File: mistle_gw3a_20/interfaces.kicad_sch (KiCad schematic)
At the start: 60 parts, among them J11 Joystick 0, J12 Joystick 1, J4 Micro_SD_Card_Det1, J5 HDMI_A, J6 Grove 1125S-4P, J8 EXT UART, SW2 KEY1, SW3 KEY2, U10 74LCX07, U9 74LCX07

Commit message: Update gw3a dev board
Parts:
- removed R13, R14: 330, Resistor_SMD:R_0402_1005Metric, symbol Device:R_Small
- removed R15, R16: 1k, Resistor_SMD:R_0402_1005Metric, symbol Device:R_Small
- removed SW2: KEY1, Button_Switch_SMD:SW_SPST_TL3342, symbol Switch:SW_Push
- removed SW3: KEY2, Button_Switch_SMD:SW_SPST_TL3342, symbol Switch:SW_Push
- added R22: 1k, Resistor_SMD:R_0402_1005Metric, symbol Device:R_Small
- added R33: 330, Resistor_SMD:R_0402_1005Metric, symbol Device:R_Small
- added SW4: KEY1, Button_Switch_SMD:SW_SPST_TL3342, symbol Switch:SW_Push
- added unit 9 of U7
- added unit 10 of U7
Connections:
- net +3.3V: now also R33.1; no longer D5.4 (VDD)
- net +5V: now also D5.4 (VDD)
- net CK+: now also U7.129 (IOL21A)
- net CK-: now also U7.130 (IOL21B)
- net D0+: now also U7.131 (IOL23A)
- net D0-: now also U7.134 (IOL23B)
- net D1+: now also U7.133 (IOL25A)
- net D1-: now also U7.135 (IOL25B)
- net D2+: now also U7.136 (IOL27A)
- net D2-: now also U7.137 (IOL27B)
- net GND: now also R22.2
- net JOYA0: now also U7.112 (IOL3A/GCLKT_14/LPLL0_T_IN2/LPLL0_T_FB0)
- net JOYA1: now also U7.111 (IOL3B/GCLKC_14/LPLL0_C_IN2/LPLL0_C_FB0)
- net JOYA2: now also U7.114 (IOL5A/GCLKT_13/LPLL0_T_IN1/LPLL0_T_FB1)
- net JOYA3: now also U7.113 (IOL5B/GCLKC_13/LPLL0_C_IN1/LPLL0_C_FB1)
- net JOYA4: now also U7.116 (IOL7A)
- net JOYA5: now also U7.115 (IOL7B)
- net JOYB0: now also U7.118 (IOL9A)
- net JOYB1: now also U7.119 (IOL9B)
- net JOYB2: now also U7.120 (IOL12A)
- net JOYB3: now also U7.121 (IOL12B)
- net JOYB4: now also U7.122 (IOL14A/LPLL1_T_IN1/LPLL1_T_FB1)
- net JOYB5: now also U7.123 (IOL14B/LPLL1_C_IN1/LPLL1_C_FB1)
- net LED0: now also U7.105 (IOT3A/GCLKT_16)
- net LED1: now also U7.106 (IOT3B/GCLKC_16)
- net LED2: now also U7.104 (IOT5A)
- net LED3: now also U7.102 (IOT19A)
- net LED4: now also U7.101 (IOT19B)
- net LED5: now also U7.99 (IOT25A)
- net MON_RX: now also U7.98 (IOT25B)
- net WS2812: now also U7.97 (IOT27A)
- new net: R33.2, SW4.1
- new net ~{USER}: R22.1, SW4.2, U7.96 (IOT27B)
- no-connect marks 3 -> 7
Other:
- moved on the sheet: C18, C19, C20, C21, C22, C23, C24, C25, C26, C40, C45, C58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

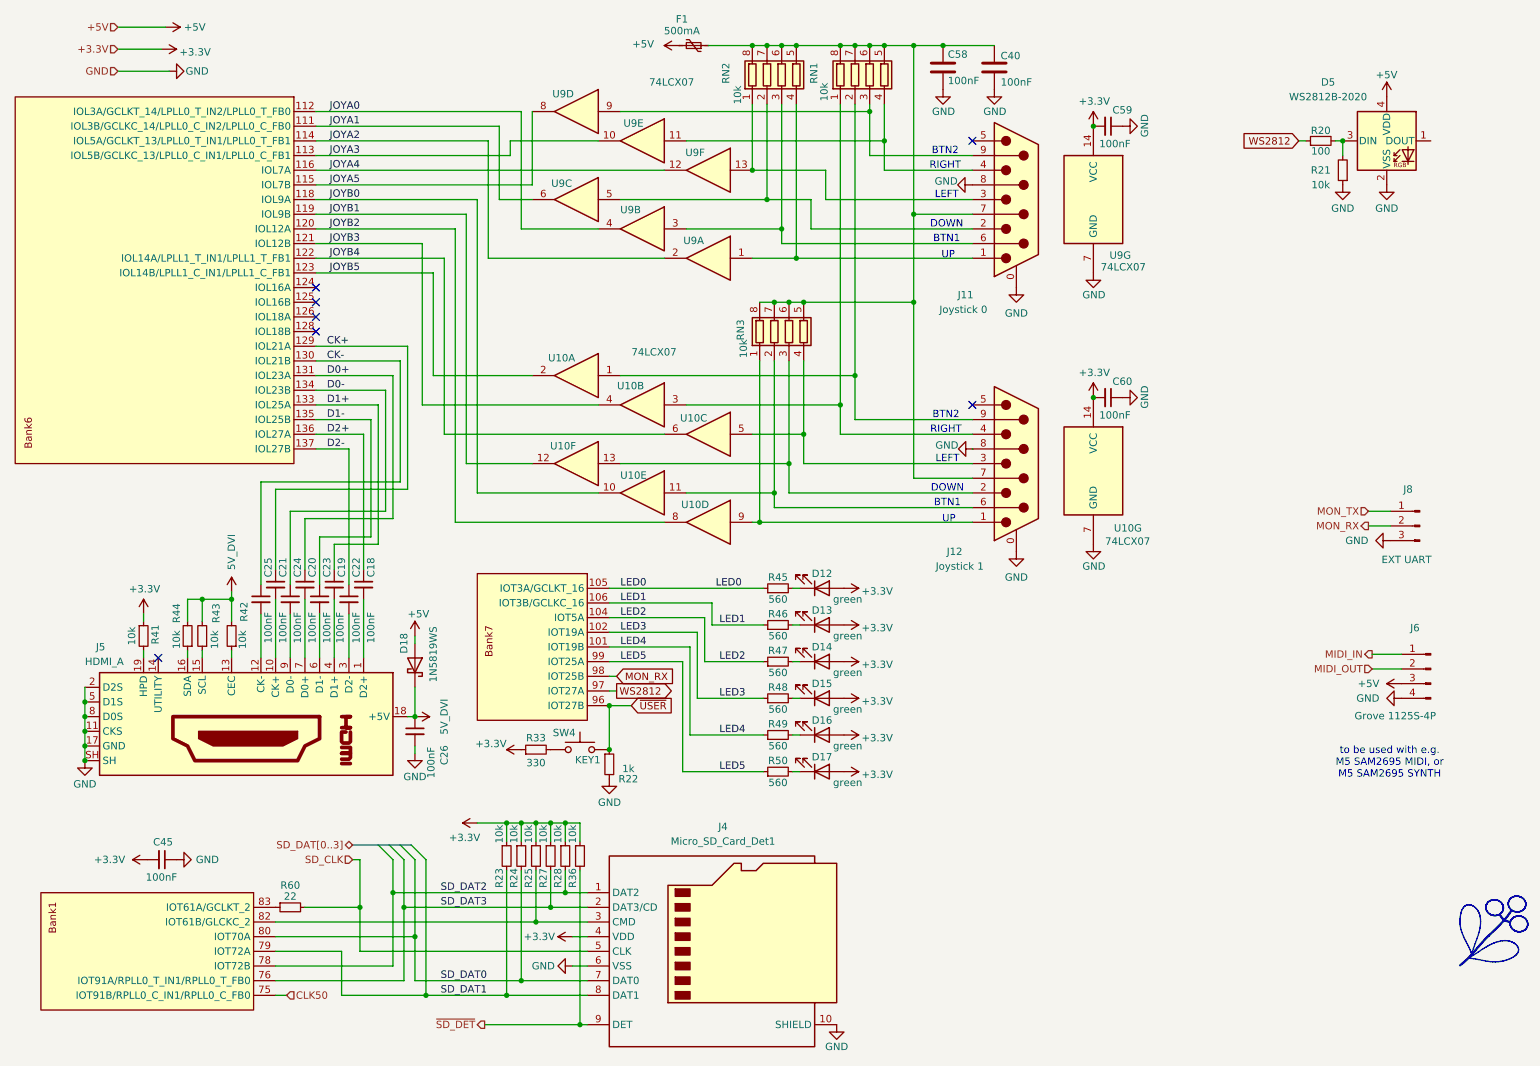
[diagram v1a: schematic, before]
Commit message: Update gw3a 20 dev board
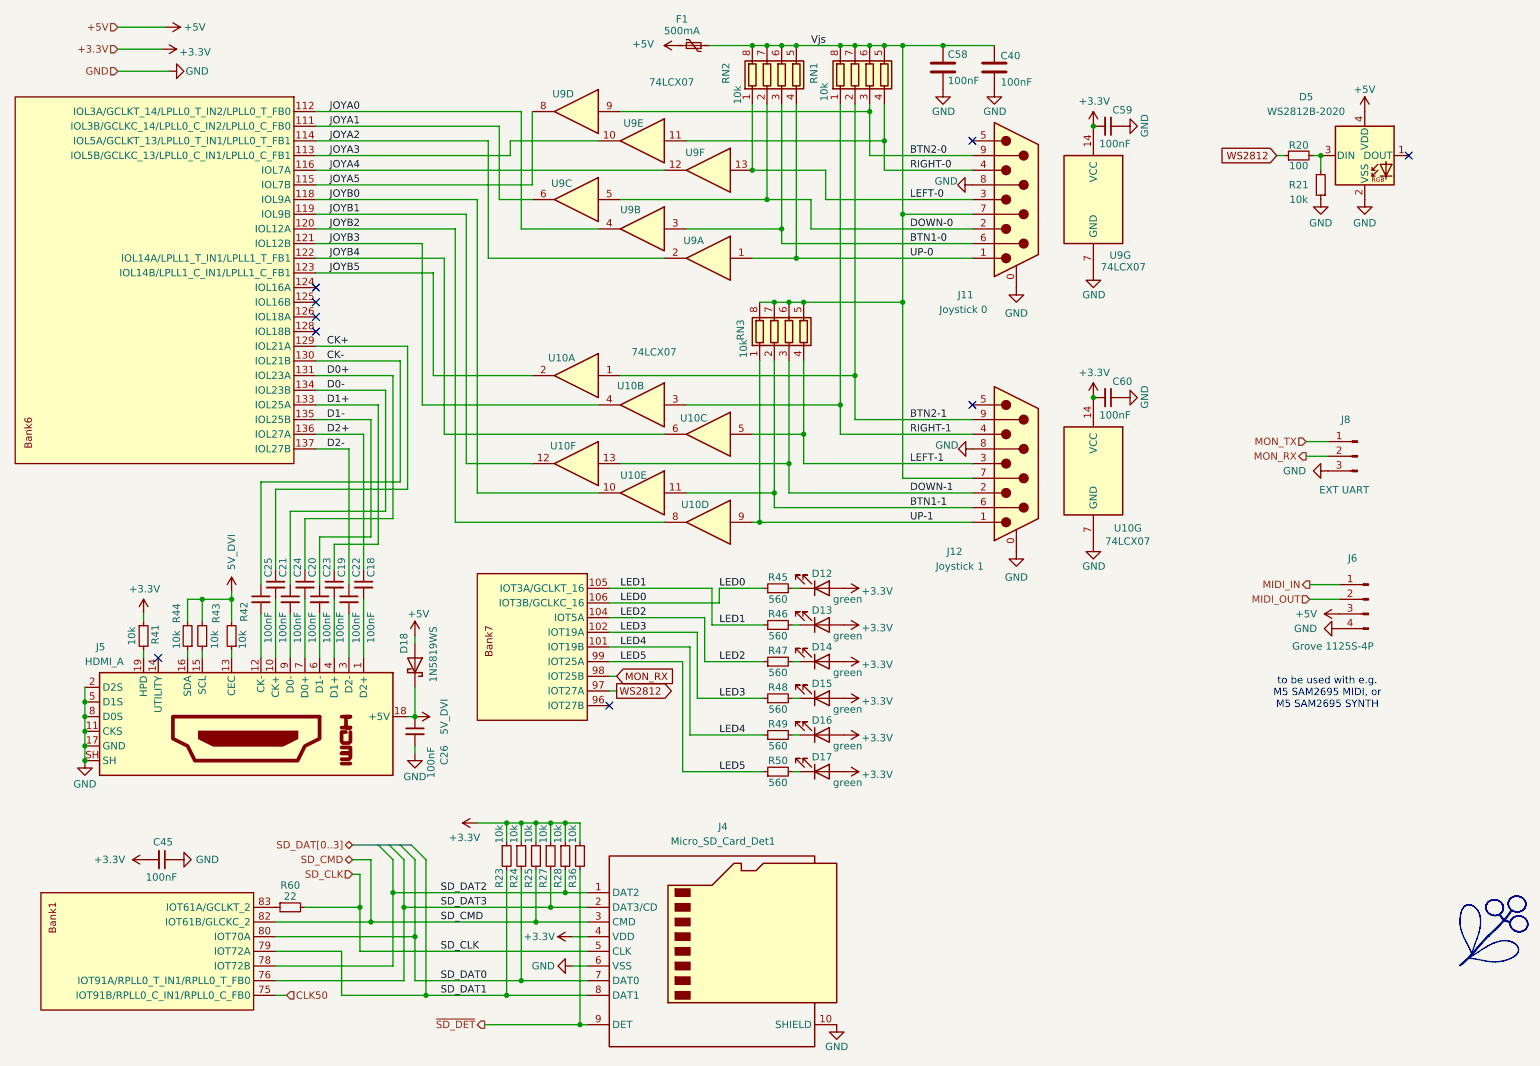
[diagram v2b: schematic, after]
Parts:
- removed R22: 1k, Resistor_SMD:R_0402_1005Metric, symbol Device:R_Small
- removed R33: 330, Resistor_SMD:R_0402_1005Metric, symbol Device:R_Small
- removed SW4: KEY1, Button_Switch_SMD:SW_SPST_TL3342, symbol Switch:SW_Push
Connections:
- net LED0: now also U7.106 (IOT3B/GCLKC_16); no longer U7.105 (IOT3A/GCLKT_16)
- net LED1: now also U7.105 (IOT3A/GCLKT_16); no longer U7.106 (IOT3B/GCLKC_16)
- net BTN1-1: now reaches J12.6, RN3.2 (R2.1), U10.11
- net Vjs: now reaches C40.2, C58.2, F1.1, J11.7, J12.7, RN1.5 (R4.2), RN1.6 (R3.2), RN1.7 (R2.2), RN1.8 (R1.2), RN2.5 (R4.2), RN2.6 (R3.2), RN2.7 (R2.2), RN2.8 (R1.2), RN3.5 (R4.2), RN3.6 (R3.2), RN3.7 (R2.2), RN3.8 (R1.2)
- net LEFT-0: now reaches J11.3, RN2.1 (R1.1), U9.13
- net DOWN-0: now reaches J11.2, RN2.2 (R2.1), U9.5
- net BTN1-0: now reaches J11.6, RN2.3 (R3.1), U9.3
- net UP-0: now reaches J11.1, RN2.4 (R4.1), U9.1
- net SD_CMD: now reaches J4.3 (CMD), R25.2, U7.82 (IOT61B/GLCKC_2)
- net RIGHT-1: now reaches J12.4, RN1.1 (R1.1), U10.3
- net BTN2-1: now reaches J12.9, RN1.2 (R2.1), U10.1
- net DOWN-1: now reaches J12.2, RN3.3 (R3.1), U10.13
- net BTN2-0: now reaches J11.9, RN1.3 (R3.1), U9.9
- net RIGHT-0: now reaches J11.4, RN1.4 (R4.1), U9.11
- net UP-1: now reaches J12.1, RN3.1 (R1.1), U10.9
- net LEFT-1: now reaches J12.3, RN3.4 (R4.1), U10.5
- net ~{USER}: no longer names the net of U7.96 (IOT27B)
- no-connect marks 7 -> 9
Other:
- note removed: "BTN1"
- note removed: "BTN2"
- note removed: "DOWN"
- note removed: "LEFT"
- note removed: "RIGHT"
- note removed: "UP"
- moved on the sheet: D5, J6, J8, R20, R21

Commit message: Update gw3a dev board
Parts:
- C18, C19, C20, C21, C22, C23, C24, C25, C26, C40, C45, C58, C59, C60, D12, D13, D14, D15, D16, D17, D18, D5, F1, J11, J12, J4, J5, R20, R21, R23, R24, R25, R27, R28, R36, R41, R42, R43, R44, R45, R46, R47, R48, R49, R50, R60, RN1, RN2, RN3, U10, U9: checked once -> (none)
- U7: value (none) -> GW3A-LV20-Q144

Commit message: Update gw3a board
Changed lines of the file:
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@@
 		(in_pos_files yes)
 		(dnp no)
-		(fields_autoplaced yes)
 		(property "Reference" "U7"
 			(at 4.064 92.456 0)
@@
 		)
 		(property "Value" "GW3A-LV20-Q144"
-			(at 46.99 63.5 0)
+			(at 32.766 94.234 0)
 			(show_name no)
 			(do_not_autoplace no)
@@
 		)
 		(property "Value" "GW3A-LV20-Q144"
-			(at 45.085 175.895 0)
-			(show_name no)
-			(do_not_autoplace no)
+			(at 36.068 188.976 0)
+			(show_name no)
+			(do_not_autoplace no)

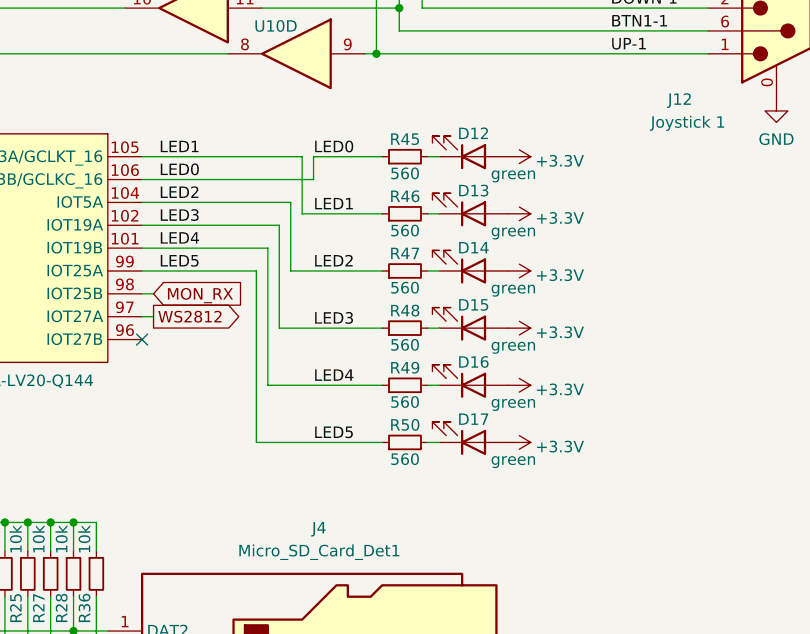
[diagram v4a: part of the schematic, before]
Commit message: Update mistle-gw3a board for rp2350
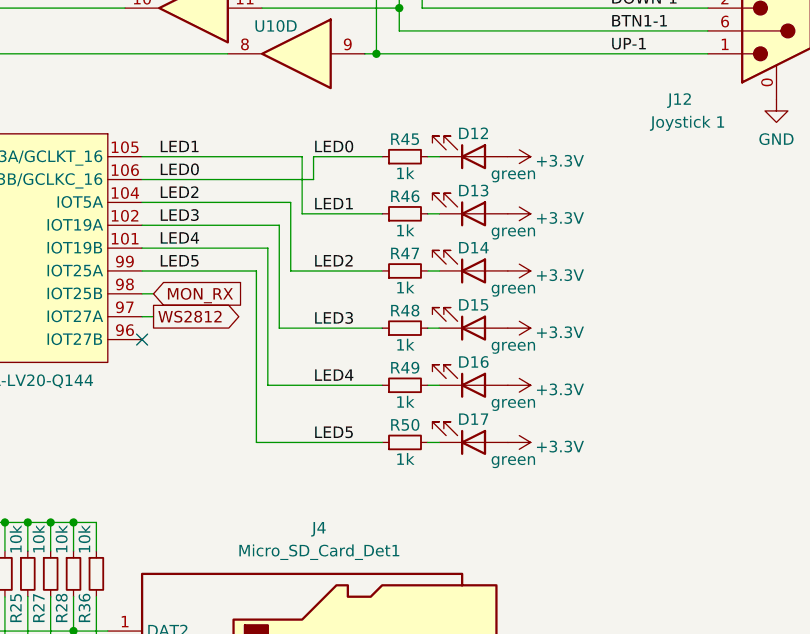
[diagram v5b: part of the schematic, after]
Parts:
- R45, R46, R47, R48, R49, R50: value 560 -> 1k; LCSC Part # C163460 -> C11702
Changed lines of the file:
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@@
 			)
 		)
-		(property "Value" "560"
+		(property "Value" "1k"
 			(at 153.67 128.905 90)
 			(show_name no)
@@
 			)
 		)
-		(property "LCSC Part #" "C163460"
+		(property "LCSC Part #" "C11702"
 			(at 153.67 127 90)
 			(hide yes)
@@
 			)
 		)
-		(property "Value" "560"
+		(property "Value" "1k"
 			(at 153.67 147.955 90)
 			(show_name no)
@@
 			)
 		)
-		(property "LCSC Part #" "C163460"
+		(property "LCSC Part #" "C11702"
 			(at 153.67 146.05 90)
 			(hide yes)
@@
 			)
 		)
-		(property "Value" "560"
+		(property "Value" "1k"
 			(at 153.67 122.555 90)
 			(show_name no)
@@
 			)
 		)
-		(property "LCSC Part #" "C163460"
+		(property "LCSC Part #" "C11702"
 			(at 153.67 120.65 90)
 			(hide yes)
@@
 			)
 		)
-		(property "Value" "560"
+		(property "Value" "1k"
 			(at 153.67 135.255 90)
 			(show_name no)
@@
 			)
 		)
-		(property "LCSC Part #" "C163460"
+		(property "LCSC Part #" "C11702"
 			(at 153.67 133.35 90)
 			(hide yes)
@@
 			)
 		)
-		(property "Value" "560"
+		(property "Value" "1k"
 			(at 153.67 116.205 90)
 			(show_name no)
@@
 			)
 		)
-		(property "LCSC Part #" "C163460"
+		(property "LCSC Part #" "C11702"
 			(at 153.67 114.3 90)
 			(hide yes)
@@
 			)
 		)
-		(property "Value" "560"
+		(property "Value" "1k"
 			(at 153.67 141.605 90)
 			(show_name no)
@@
 			)
 		)
-		(property "LCSC Part #" "C163460"
+		(property "LCSC Part #" "C11702"
 			(at 153.67 139.7 90)
 			(hide yes)

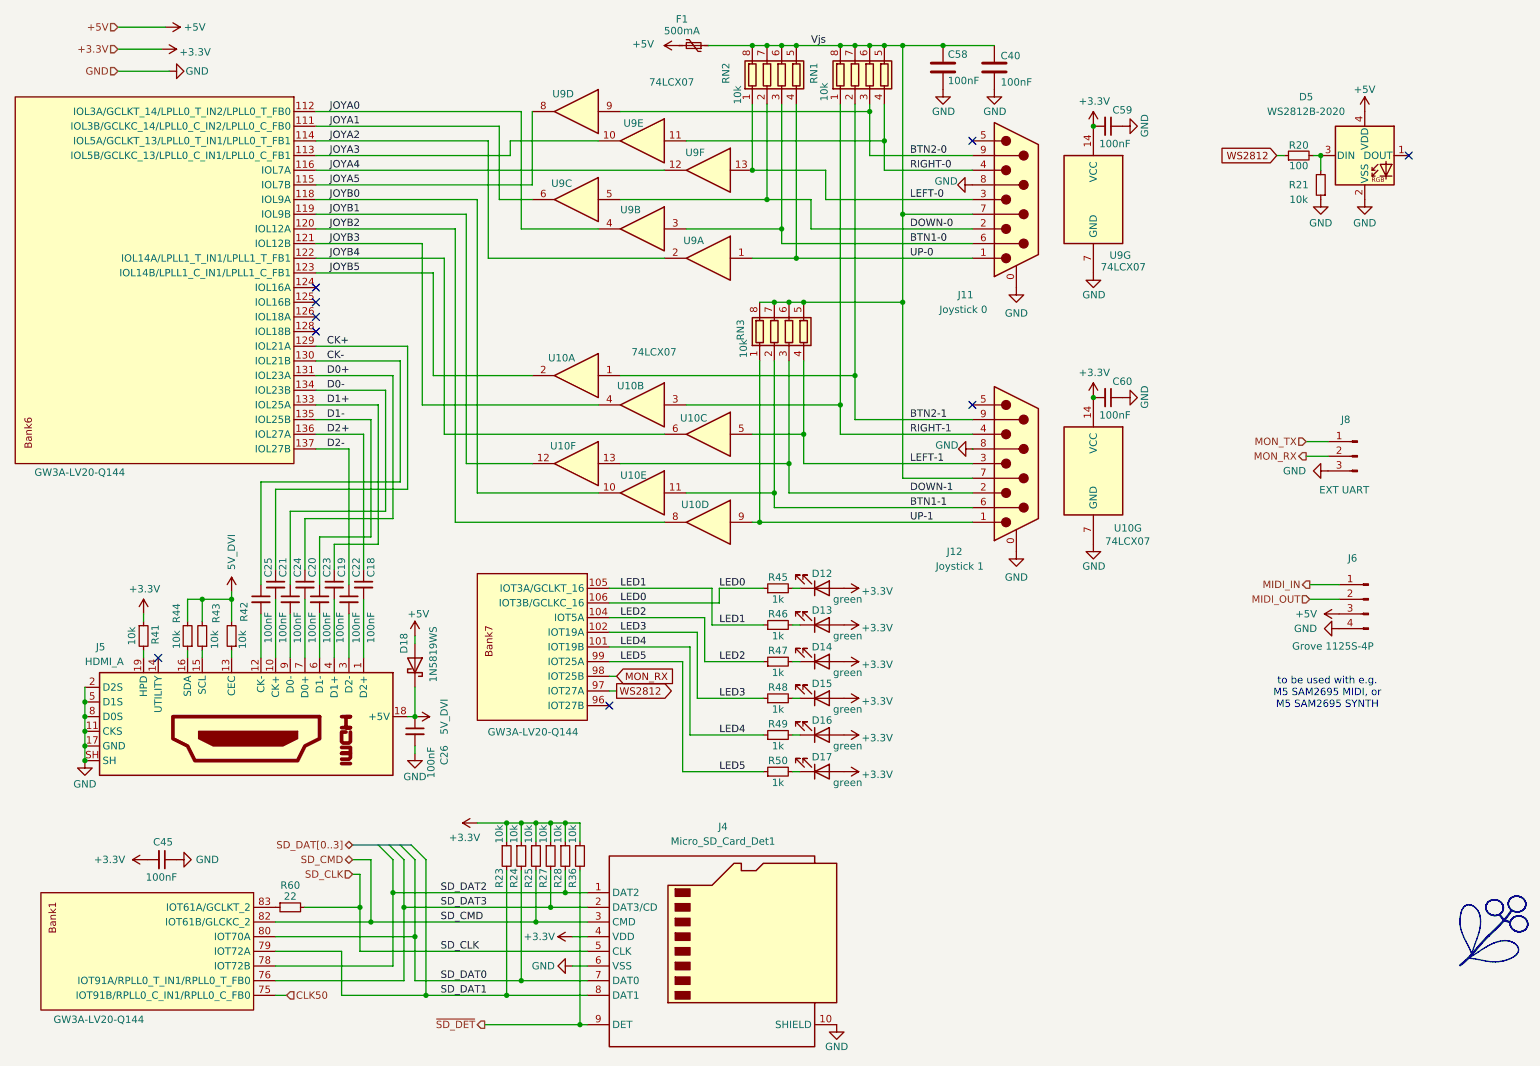
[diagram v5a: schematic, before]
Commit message: Add expansion connector
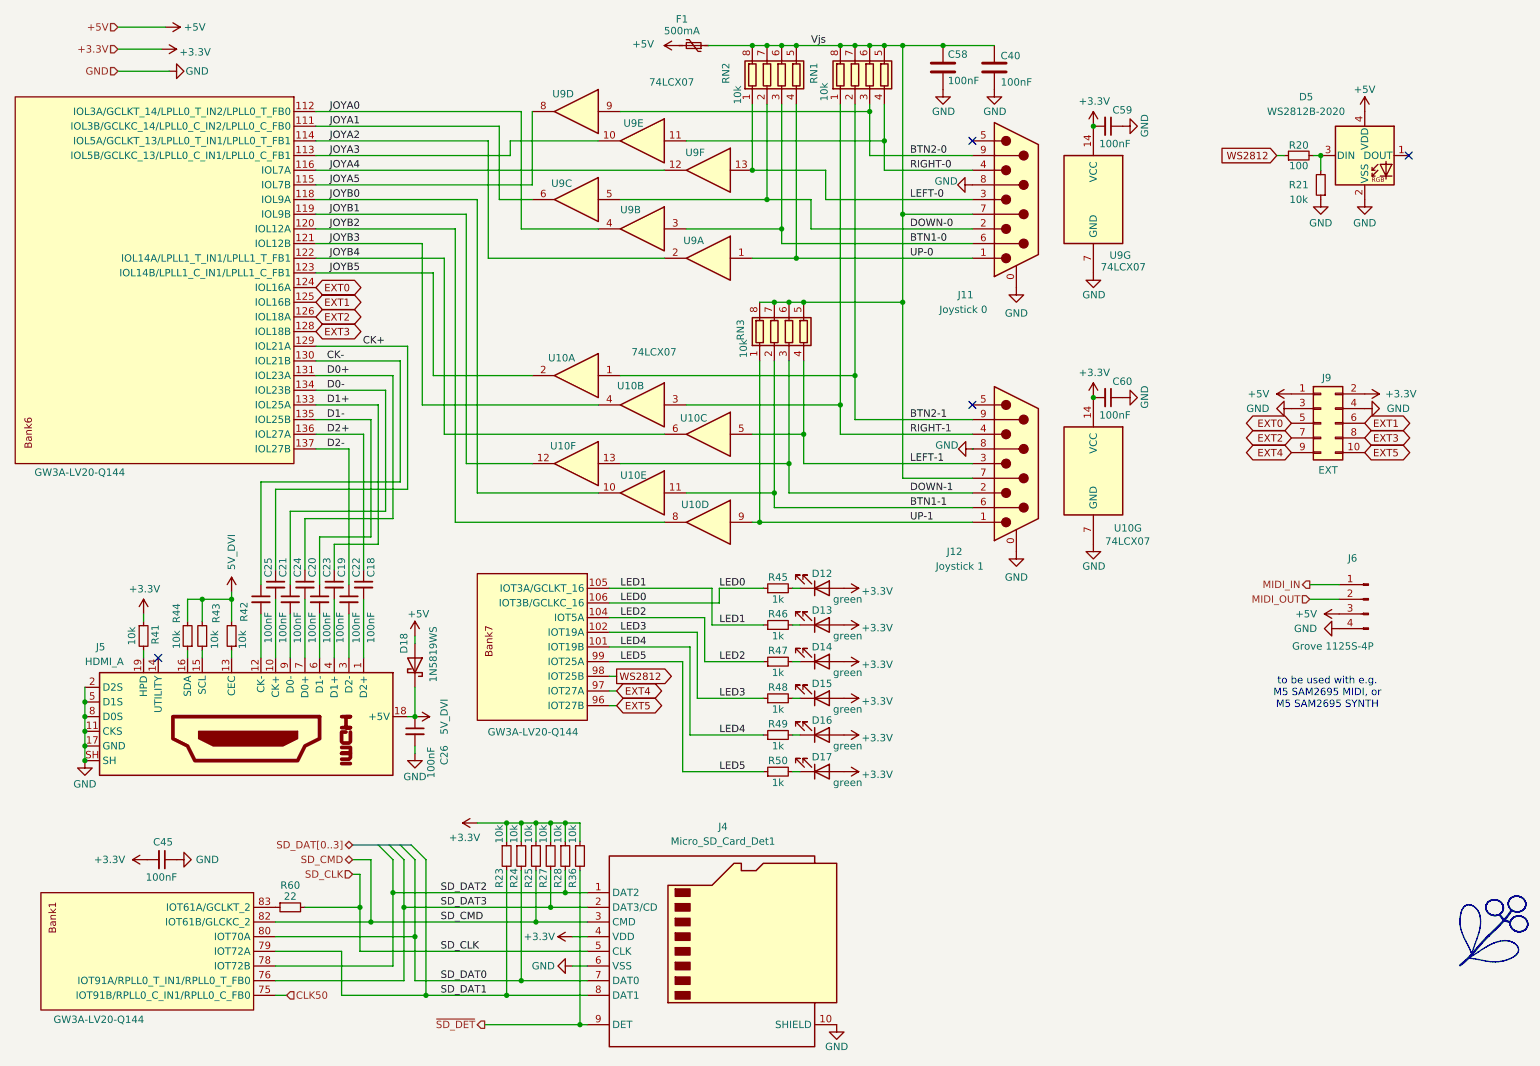
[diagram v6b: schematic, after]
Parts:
- removed J8: EXT UART, Connector_PinHeader_2.54mm:PinHeader_1x03_P2.54mm_Vertical, symbol Connector:Conn_01x03_Pin
- added J9: EXT, Connector_IDC:IDC-Header_2x05_P2.54mm_Vertical, symbol Connector_Generic:Conn_02x05_Odd_Even
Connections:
- net MON_RX is gone; now on net WS2812: U7.98 (IOT25B)
- net +3.3V: now also J9.2 (Pin_2)
- net +5V: now also J9.1 (Pin_1)
- net GND: now also J9.3 (Pin_3), J9.4 (Pin_4)
- net WS2812: no longer U7.97 (IOT27A)
- net EXT0: now reaches U7.124 (IOL16A)
- net EXT0: now also J9.5 (Pin_5)
- net EXT1: now reaches U7.125 (IOL16B)
- net EXT1: now also J9.6 (Pin_6)
- net EXT2: now reaches U7.126 (IOL18A)
- net EXT2: now also J9.7 (Pin_7)
- net EXT3: now reaches U7.128 (IOL18B)
- net EXT3: now also J9.8 (Pin_8)
- net EXT5: now reaches U7.96 (IOT27B)
- net EXT5: now also J9.10 (Pin_10)
- new net EXT4: J9.9 (Pin_9), U7.97 (IOT27A)
- no-connect marks 9 -> 4
